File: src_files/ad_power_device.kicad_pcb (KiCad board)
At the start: 2 copper layers, 88.9 x 56.6 mm, 199 parts, among them J1 SPEAKER, J2 5622-6309-ML, U1 RK3566, U2 RK809, U3 AP6256, U4 LPDDRS_32_IS43LQ32128A-062BLI, U5 TLV62569DDC, U6 TLV62569DDC, Y1 32.768KHz, Y2 37.4MHz_10PPM, Y3 24MHz/10ppm

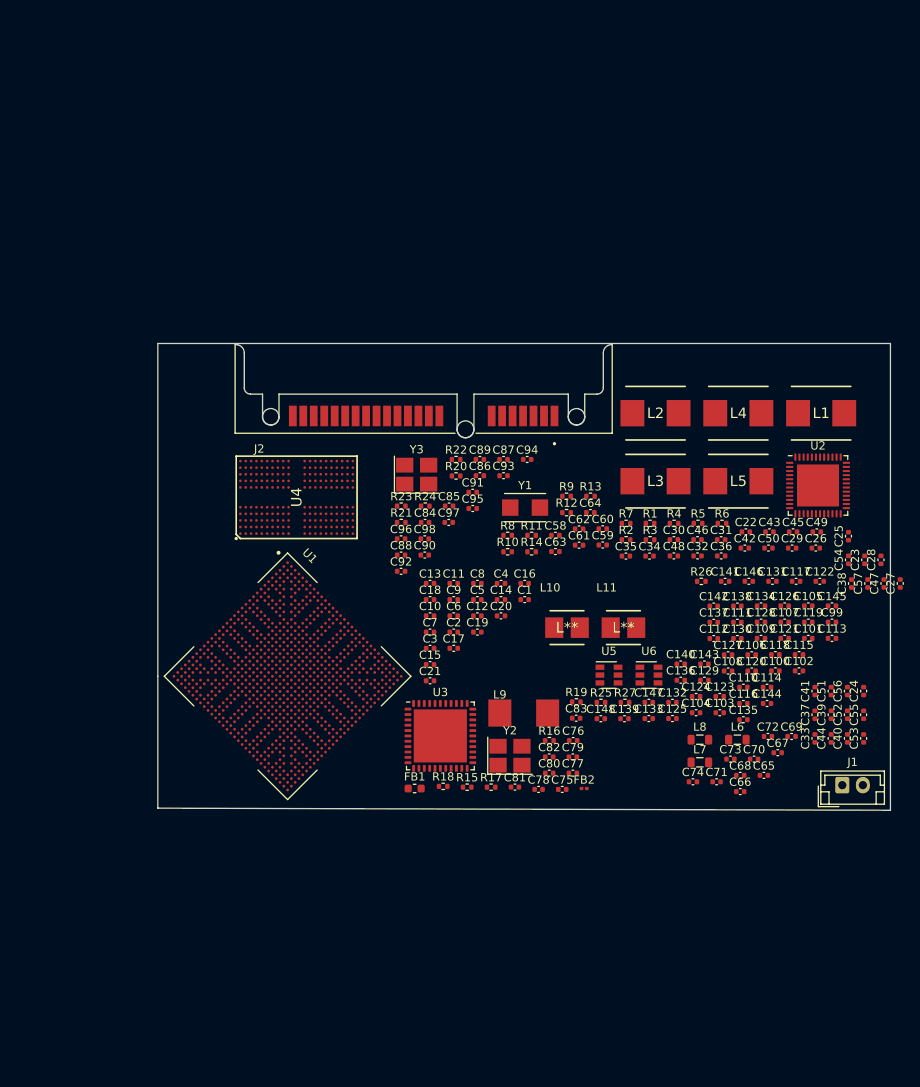
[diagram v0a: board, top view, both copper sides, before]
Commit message: added 3 screens
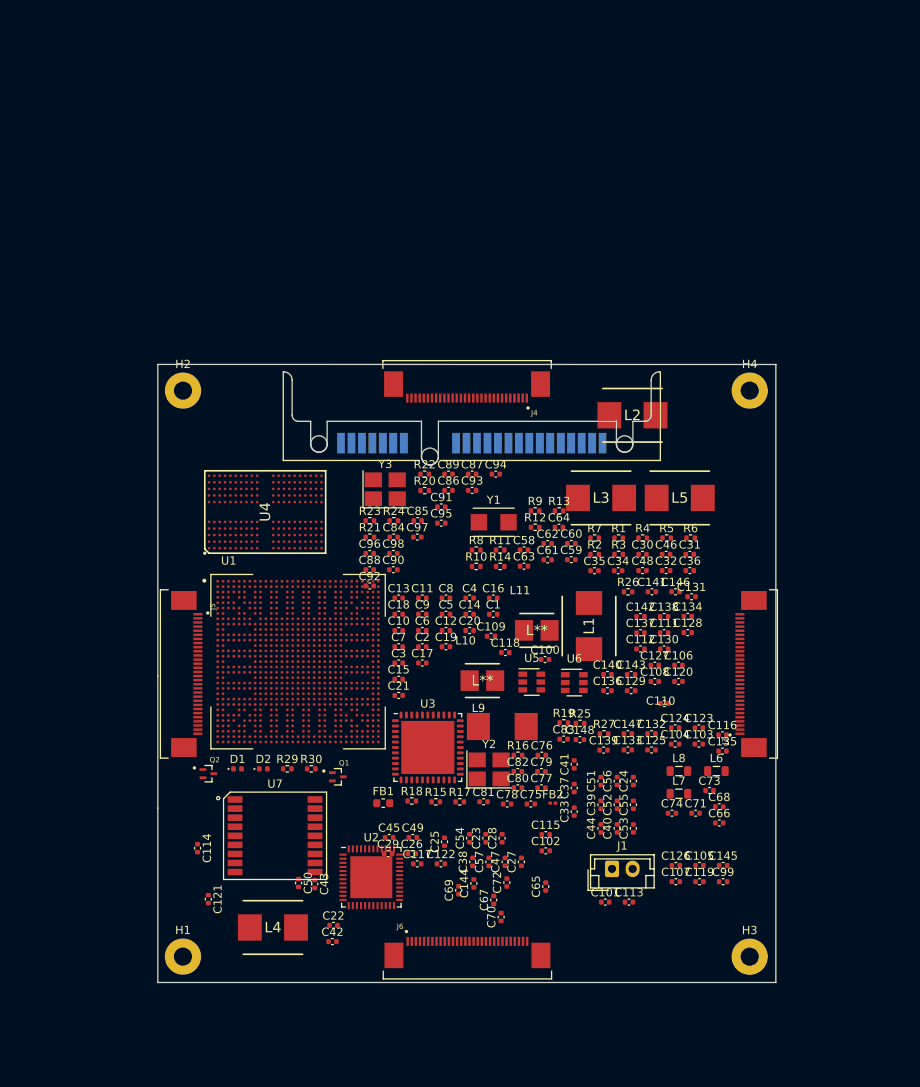
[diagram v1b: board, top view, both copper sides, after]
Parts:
- added D1: LED, LED_SMD:LED_0402_1005Metric, F.Cu at (22.4, 192.6)
- added D2: LED, LED_SMD:LED_0402_1005Metric, F.Cu at (25.5, 192.6)
- added H1: MountingHole, MountingHole:MountingHole_2.2mm_M2_Pad, F.Cu at (15.8, 215.4)
- added H2: MountingHole, MountingHole:MountingHole_2.2mm_M2_Pad, F.Cu at (15.8, 146.7)
- added H3: MountingHole, MountingHole:MountingHole_2.2mm_M2_Pad, F.Cu at (84.5, 215.4)
- added H4: MountingHole, MountingHole:MountingHole_2.2mm_M2_Pad, F.Cu at (84.5, 146.7)
- added J3: 3-1734592-0, greencharge-footprints:TE_3-1734592-0, F.Cu at (83.3, 181.1)
- added J4: 3-1734592-0, greencharge-footprints:TE_3-1734592-0, F.Cu at (50.2, 147.6)
- added J5: 3-1734592-0, greencharge-footprints:TE_3-1734592-0, F.Cu at (17.6, 181.1)
- added J6: 3-1734592-0, greencharge-footprints:TE_3-1734592-0, F.Cu at (50.3, 213.5)
- added Q1: DTC143ZEBTL, greencharge-footprints:SOTFL50P160X85-3N, F.Cu at (34.5, 193.5)
- added Q2: DTC143ZEBTL, greencharge-footprints:SOTFL50P160X85-3N, F.Cu at (18.8, 193.2)
- added R29: 1K, Resistor_SMD:R_0402_1005Metric, F.Cu at (28.4, 192.6)
- added R30: 1K, Resistor_SMD:R_0402_1005Metric, F.Cu at (31.3, 192.6)
- added U7: QUECTEL_L70-RL, greencharge-footprints:QUECTEL_L70-R, F.Cu at (26.4, 201.2)
- J2: moved to B.Cu
- moved L4 84.2 mm to (26.7, 211.8)
- moved C121 76.8 mm to (18.8, 208.4), turned to 270 degrees
- moved U2 72.1 mm to (38.6, 205.7)
- moved C114 71.8 mm to (17.5, 202.2), turned to 270 degrees
- moved C50 70.0 mm to (29.8, 206.4), turned to 270 degrees
- moved C43 69.8 mm to (31.8, 206.6), turned to 270 degrees
- moved C42 69.2 mm to (33.9, 213.6)
- moved C22 69.2 mm to (34.0, 211.6)
- moved C26 61.5 mm to (43.5, 202.9)
- moved C45 61.5 mm to (40.8, 200.9)
- moved C29 61.5 mm to (40.7, 202.9)
- moved C49 61.5 mm to (43.6, 200.9)
- moved C25 61.5 mm to (47.5, 201.4)
- moved C117 57.4 mm to (44.2, 204.1)
- moved C122 57.4 mm to (47.1, 204.1)
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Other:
- board size 88.9 x 56.6 mm -> 75 x 75 mm

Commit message: schematic capture complete
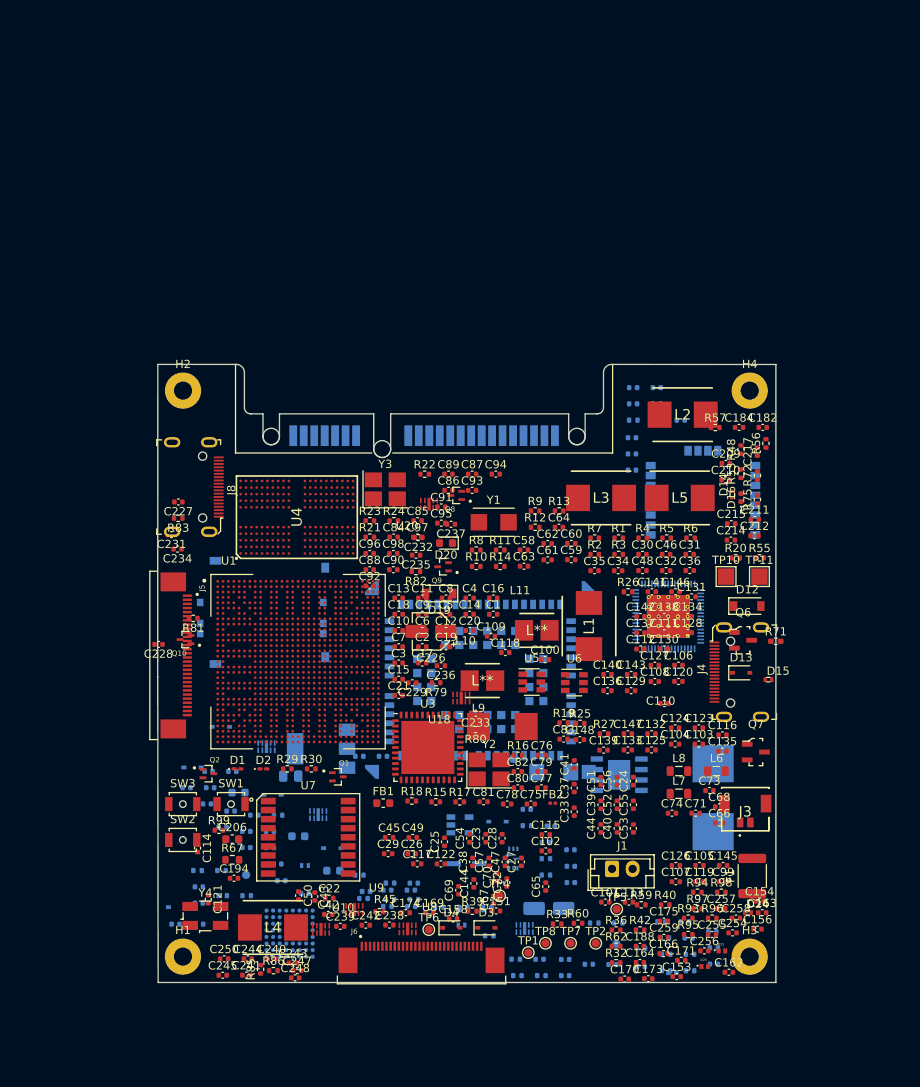
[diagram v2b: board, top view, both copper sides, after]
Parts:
- added C149: 10uF, Capacitor_SMD:C_0402_1005Metric, B.Cu at (70.2, 152.4)
- added C150: 100nF, Capacitor_SMD:C_0402_1005Metric, B.Cu at (73.2, 146.3)
- added C151: 4.7uF, Capacitor_SMD:C_0402_1005Metric, F.Cu at (53.8, 209.8)
- added C152: 4.7uF, Capacitor_SMD:C_0402_1005Metric, B.Cu at (76.7, 211.1)
- added C153: 1uF, Capacitor_SMD:C_0402_1005Metric, F.Cu at (75.7, 217.8)
- added C154: 1uF, Capacitor_SMD:C_0402_1005Metric, F.Cu at (85.7, 208.6)
- added C155: 1uF, Capacitor_SMD:C_0402_1005Metric, B.Cu at (75.1, 217.3)
- added C156: 1uF, Capacitor_SMD:C_0402_1005Metric, F.Cu at (85.5, 212.0)
- added C157: 100nF, Capacitor_SMD:C_0402_1005Metric, B.Cu at (67.9, 216.3)
- added C158: 100nF, Capacitor_SMD:C_0402_1005Metric, F.Cu at (48.5, 210.8)
- added C159: 100nF, Capacitor_SMD:C_0402_1005Metric, B.Cu at (71.3, 216.6)
- added C160: 100nF, Capacitor_SMD:C_0402_1005Metric, B.Cu at (17.7, 211.4)
- added C161: 100nF, Capacitor_SMD:C_0402_1005Metric, B.Cu at (62.1, 215.7)
- added C162: 100nF, Capacitor_SMD:C_0402_1005Metric, F.Cu at (82.0, 217.3)
- added C163: 100nF, Capacitor_SMD:C_0402_1005Metric, F.Cu at (86.0, 210.0)
- added C164: 10uF, Capacitor_SMD:C_0402_1005Metric, F.Cu at (71.2, 216.1)
- added C165: 10uF, Capacitor_SMD:C_0402_1005Metric, B.Cu at (65.0, 216.3)
- added C166: 100nF, Capacitor_SMD:C_0402_1005Metric, F.Cu at (74.1, 215.0)
- added C167: 10uF, Capacitor_SMD:C_0402_1005Metric, B.Cu at (80.0, 212.3)
- added C168: 100nF, Capacitor_SMD:C_0402_1005Metric, B.Cu at (14.9, 211.4)
- added C169: 10uF, Capacitor_SMD:C_0402_1005Metric, F.Cu at (45.7, 210.0)
- added C170: 100nF, Capacitor_SMD:C_0402_1005Metric, F.Cu at (69.4, 218.1)
- added C171: 100nF, Capacitor_SMD:C_0402_1005Metric, F.Cu at (76.2, 215.8)
- added C172: 100nF, Capacitor_SMD:C_0402_1005Metric, B.Cu at (80.2, 214.3)
- added C173: 100nF, Capacitor_SMD:C_0402_1005Metric, F.Cu at (72.2, 218.1)
- added C174: 100nF, Capacitor_SMD:C_0402_1005Metric, F.Cu at (42.8, 210.0)
- added C175: 100nF, Capacitor_SMD:C_0402_1005Metric, F.Cu at (74.1, 211.1)
- added C176: 1uF, Capacitor_SMD:C_0402_1005Metric, B.Cu at (62.1, 217.7)
- added C177: 100nF, Capacitor_SMD:C_0402_1005Metric, B.Cu at (76.2, 150.3)
- added C178: 220pF, Capacitor_SMD:C_0402_1005Metric, B.Cu at (70.2, 154.4)
- added C179: 220pF, Capacitor_SMD:C_0402_1005Metric, B.Cu at (73.2, 148.3)
- added C180: 180pF, Capacitor_SMD:C_0402_1005Metric, B.Cu at (70.4, 146.3)
- added C181: 180pF, Capacitor_SMD:C_0402_1005Metric, B.Cu at (70.2, 156.3)
- added C182: 66pF, Capacitor_SMD:C_0402_1005Metric, F.Cu at (86.1, 151.2)
- added C183: 100nF, Capacitor_SMD:C_0402_1005Metric, B.Cu at (73.3, 150.3)
- added C184: 4.7uF, Capacitor_SMD:C_0402_1005Metric, F.Cu at (83.2, 151.2)
- added C185: 100nF, Capacitor_SMD:C_0402_1005Metric, B.Cu at (70.4, 148.3)
- added C186: 4.7uF, Capacitor_SMD:C_0402_1005Metric, B.Cu at (77.1, 213.1)
- added C187: 4.7uF, Capacitor_SMD:C_0402_1005Metric, B.Cu at (80.2, 216.3)
- added C188: 100nF, Capacitor_SMD:C_0402_1005Metric, F.Cu at (71.2, 214.1)
- added C189: 100nF, Capacitor_SMD:C_0402_1005Metric, B.Cu at (59.0, 215.7)
- added C190: 1uF, Capacitor_SMD:C_0402_1005Metric, B.Cu at (73.8, 211.1)
- added C191: 0.1uF, Capacitor_SMD:C_0402_1005Metric, B.Cu at (23.4, 200.2)
- added C192: 0.1uF, Capacitor_SMD:C_0402_1005Metric, B.Cu at (18.7, 196.8)
- added C193: 0.1uF, Capacitor_SMD:C_0402_1005Metric, B.Cu at (20.6, 199.7)
- added C194: 22pF, Capacitor_SMD:C_0402_1005Metric, F.Cu at (21.9, 205.9)
- added C195: 22pF, Capacitor_SMD:C_0402_1005Metric, B.Cu at (16.2, 194.9)
- added C196: 0.1uF, Capacitor_SMD:C_0402_1005Metric, B.Cu at (23.4, 202.1)
- added C197: 0.1uF, Capacitor_SMD:C_0402_1005Metric, B.Cu at (27.2, 204.1)
- added C198: 0.1uf, Capacitor_SMD:C_0402_1005Metric, B.Cu at (27.7, 206.2)
- added C199: 0.1uF, Capacitor_SMD:C_0402_1005Metric, B.Cu at (26.3, 200.2)
- added C200: 0.1uF, Capacitor_SMD:C_0402_1005Metric, B.Cu at (19.1, 194.9)
- added C201: 0.1uF, Capacitor_SMD:C_0402_1005Metric, B.Cu at (21.7, 192.9)
- added C202: 0.1uF, Capacitor_SMD:C_0402_1005Metric, B.Cu at (21.5, 197.7)
- added C203: 0.1uF, Capacitor_SMD:C_0402_1005Metric, B.Cu at (18.9, 192.9)
- added C204: 2.2uF, Capacitor_SMD:C_0402_1005Metric, B.Cu at (24.4, 198.2)
- added C205: 10uF, Capacitor_SMD:C_0603_1608Metric, B.Cu at (29.7, 200.8)
- added C206: 10uF, Capacitor_SMD:C_0603_1608Metric, F.Cu at (21.7, 201.1)
- added C207: 1uF, Capacitor_SMD:C_0402_1005Metric, B.Cu at (26.3, 202.2)
- added C208: 1uF, Capacitor_SMD:C_0402_1005Metric, B.Cu at (30.6, 207.7)
- added C209: 1uF, Capacitor_SMD:C_0402_1005Metric, F.Cu at (81.6, 155.5)
- added C210: 1uF, Capacitor_SMD:C_0402_1005Metric, F.Cu at (81.6, 157.5)
- added C211: 100nF, Capacitor_SMD:C_0402_1005Metric, F.Cu at (85.1, 162.3)
- added C212: 100nF, Capacitor_SMD:C_0402_1005Metric, F.Cu at (85.1, 164.3)
- added C213: 1uF, Capacitor_SMD:C_0402_1005Metric, B.Cu at (43.4, 207.3)
- added C214: 1uF, Capacitor_SMD:C_0402_1005Metric, F.Cu at (82.2, 164.8)
- added C215: 100nF, Capacitor_SMD:C_0402_1005Metric, F.Cu at (82.3, 162.8)
- added C216: 100nF, Capacitor_SMD:C_0402_1005Metric, B.Cu at (43.5, 209.3)
- added C217: 100nF, Capacitor_SMD:C_0402_1005Metric, F.Cu at (85.4, 154.1)
- added C218: 100nF, Capacitor_SMD:C_0402_1005Metric, B.Cu at (40.5, 207.3)
- added C219: 1uF, Capacitor_SMD:C_0402_1005Metric, B.Cu at (43.8, 206.5)
- added C220: 10uF, Capacitor_SMD:C_0402_1005Metric, B.Cu at (62.8, 206.4)
- added C221: 10uF, Capacitor_SMD:C_0402_1005Metric, B.Cu at (59.8, 201.5)
- added C222: 22uF, Capacitor_SMD:C_0402_1005Metric, B.Cu at (62.8, 204.4)
- added C223: 22uF, Capacitor_SMD:C_0402_1005Metric, B.Cu at (57.5, 197.5)
- added C224: 22uF, Capacitor_SMD:C_0402_1005Metric, B.Cu at (60.4, 199.5)
- added C225: 22uF, Capacitor_SMD:C_0402_1005Metric, B.Cu at (62.8, 202.4)
- added C226: 100uF, Capacitor_SMD:CP_Elec_4x3, F.Cu at (45.8, 175.9)
- added C227: 100nF, Capacitor_SMD:C_0402_1005Metric, F.Cu at (15.2, 160.2)
- added C228: 33pF, Capacitor_SMD:C_0402_1005Metric, F.Cu at (12.8, 177.5)
- added C229: 10pF, Capacitor_SMD:C_0402_1005Metric, F.Cu at (43.6, 182.1)
- added C230: 100uF, Capacitor_SMD:CP_Elec_4x3, B.Cu at (60.2, 209.5)
- added C231: 100nF, Capacitor_SMD:C_0402_1005Metric, F.Cu at (14.4, 164.2)
- added C232: 33pF, Capacitor_SMD:C_0402_1005Metric, F.Cu at (44.3, 164.5)
- added C233: 10pF, Capacitor_SMD:C_0402_1005Metric, F.Cu at (51.3, 185.8)
- added C234: 33pF, Capacitor_SMD:C_0402_1005Metric, F.Cu at (15.1, 165.9)
- added C235: 33pF, Capacitor_SMD:C_0402_1005Metric, F.Cu at (44.0, 166.7)
- added C236: 100nF, Capacitor_SMD:C_0402_1005Metric, F.Cu at (47.1, 180.1)
- added C237: 33pF, Capacitor_SMD:C_0402_1005Metric, F.Cu at (48.3, 162.9)
- added C238: 100nF, Capacitor_SMD:C_0402_1005Metric, F.Cu at (40.8, 211.5)
- added C239: 4.7uF, Capacitor_SMD:C_0402_1005Metric, F.Cu at (34.8, 211.7)
- added C240: 100nF, Capacitor_SMD:C_0402_1005Metric, F.Cu at (26.5, 215.6)
- added C241: 100nF, Capacitor_SMD:C_0402_1005Metric, F.Cu at (23.4, 217.6)
- added C242: 4.7uF, Capacitor_SMD:C_0402_1005Metric, F.Cu at (37.9, 211.6)
- added C243: 100nF, Capacitor_SMD:C_0402_1005Metric, F.Cu at (29.1, 216.2)
- added C244: 100nF, Capacitor_SMD:C_0402_1005Metric, F.Cu at (23.6, 215.6)
- added C245: 100nF, Capacitor_SMD:C_0402_1005Metric, F.Cu at (20.6, 217.6)
- added C246: 1nF_50V, Capacitor_SMD:C_0402_1005Metric, B.Cu at (17.7, 208.9)
- added C247: 1nF_50V, Capacitor_SMD:C_0402_1005Metric, F.Cu at (29.6, 217.1)
- added C248: 1nF_50V, Capacitor_SMD:C_0402_1005Metric, F.Cu at (29.4, 217.9)
- added C249: 1nF_50V, Capacitor_SMD:C_0402_1005Metric, B.Cu at (17.7, 206.9)
- added C250: 100nF, Capacitor_SMD:C_0402_1005Metric, F.Cu at (20.8, 215.6)
- added C251: 130pF, Capacitor_SMD:C_0402_1005Metric, B.Cu at (42.9, 191.1)
- added C252: 1uF, Capacitor_SMD:C_0402_1005Metric, B.Cu at (37.2, 191.1)
- added C253: 1uF, Capacitor_SMD:C_0402_1005Metric, B.Cu at (40.0, 191.1)
- added C254: 47uF_10V, Capacitor_SMD:C_0402_1005Metric, F.Cu at (82.4, 212.5)
- added C255: 47uF_10V, Capacitor_SMD:C_0402_1005Metric, F.Cu at (80.0, 212.7)
- added C256: 22uF_10V, Capacitor_SMD:C_0402_1005Metric, F.Cu at (79.0, 214.7)
- added C257: 22uF_10V, Capacitor_SMD:C_0402_1005Metric, F.Cu at (81.1, 209.5)
- added C258: 100nF, Capacitor_SMD:C_0402_1005Metric, F.Cu at (82.9, 210.7)
- added C259: 100nF, Capacitor_SMD:C_0402_1005Metric, F.Cu at (74.1, 213.0)
- added D10: 1N5819WS, Diode_SMD:D_SOD-323, B.Cu at (16.9, 192.4)
- added D11: ESD5451R-2/TR, greencharge-footprints:DFP1006-2L, B.Cu at (29.4, 202.8)
- added D12: SMF11A, Diode_SMD:D_SOD-123, F.Cu at (84.2, 172.8)
- added D13: 1N5819WS, Diode_SMD:D_SOD-323, F.Cu at (83.5, 180.9)
- added D14: ESD5451R-2/TR, greencharge-footprints:DFP1006-2L, F.Cu at (80.9, 158.1)
- added D15: ESD5451R-2/TR, greencharge-footprints:DFP1006-2L, F.Cu at (88.0, 180.2)
- added D16: LED, LED_SMD:LED_0402_1005Metric, F.Cu at (83.5, 159.7)
- added D17: LED, LED_SMD:LED_0402_1005Metric, B.Cu at (38.0, 207.5)
- added D18: D, Diode_SMD:D_SOD-323, B.Cu at (53.9, 199.0)
- added D19: SMF11A, Diode_SMD:D_SOD-123, F.Cu at (46.8, 171.3)
- added D20: LED, LED_SMD:LED_0603_1608Metric, F.Cu at (47.7, 165.2)
- added D21: SS56, greencharge-footprints:SMAG, B.Cu at (62.8, 193.0)
- added D22: LED, LED_SMD:LED_0603_1608Metric, B.Cu at (55.1, 191.4)
- added D23: ESD9X5VU, greencharge-footprints:ESD9X5VU_DFN1006-2, F.Cu at (81.1, 214.7)
- added D24: ESD5451R-2/TR, greencharge-footprints:DFP1006-2L, F.Cu at (85.5, 208.5)
- added D25: ESD9X5VU, greencharge-footprints:ESD9X5VU_DFN1006-2, F.Cu at (79.0, 216.6)
- added D3: 1N5819WS, Diode_SMD:D_SOD-323, F.Cu at (52.6, 211.9)
- added D4: 1N5819WS, Diode_SMD:D_SOD-323, F.Cu at (48.3, 211.9)
- added D5: 1N5819WS, Diode_SMD:D_SOD-323, B.Cu at (15.0, 209.4)
- added D6: ESD5451R-2/TR, greencharge-footprints:DFP1006-2L, B.Cu at (50.7, 213.1)
- added D7: D, Diode_SMD:D_SOD-323, B.Cu at (20.3, 187.5)
- added D8: D, Diode_SMD:D_SOD-323, B.Cu at (33.9, 202.2)
- added D9: D, Diode_SMD:D_SOD-323, B.Cu at (26.6, 195.7)
- added F1: mSMD300, Fuse:Fuse_1812_4532Metric, F.Cu at (84.8, 205.6)
- added FB3: Ferrite Bead, Inductor_SMD:L_0603_1608Metric, B.Cu at (22.5, 195.5)
- added FB4: Ferrite Bead, Inductor_SMD:L_0603_1608Metric, B.Cu at (34.0, 204.9)
- added IC1: TPS62867RQYR, greencharge-footprints:TPS62865RQYR, B.Cu at (55.8, 203.5)
- added J8: 2001-1-2-21-00-BK, digikey-footprints:HDMI_Mini_Female_2001-1-2-21-00-BK, F.Cu at (20.1, 158.4)
- added J9: SIM_Card, greencharge-footprints:MOLEX_78800-0001, B.Cu at (26.1, 173.6)
- added L12: IHLP1212AEERR22M11, greencharge-footprints:INDPM3630X150N, B.Cu at (50.1, 204.1)
- added L13: 6uH, greencharge-footprints:7443550600, B.Cu at (80.1, 192.0)
- added Q10: DTC143ZEBTL, greencharge-footprints:SOTFL50P160X85-3N, F.Cu at (16.1, 176.9)
- added Q6: DTC143ZEBTL, digikey-footprints:SOT-23-3, F.Cu at (83.7, 177.0)
- added Q7: DTC143ZEBTL, digikey-footprints:SOT-23-3, F.Cu at (85.3, 190.6)
- added Q8: DTC143ZEBTL, greencharge-footprints:SOTFL50P160X85-3N, F.Cu at (48.9, 159.4)
- added Q9: DTC143ZEBTL, greencharge-footprints:SOTFL50P160X85-3N, F.Cu at (47.3, 168.1)
- added R31: 0R, Resistor_SMD:R_0402_1005Metric, B.Cu at (71.3, 214.3)
- added R32: 0R, Resistor_SMD:R_0402_1005Metric, F.Cu at (68.3, 216.1)
- added R33: 1R_1%, Resistor_SMD:R_0402_1005Metric, F.Cu at (61.2, 211.4)
- added R34: 1R_1%, Resistor_SMD:R_0402_1005Metric, B.Cu at (56.3, 217.7)
- added R35: 1R_1%, Resistor_SMD:R_0402_1005Metric, B.Cu at (52.7, 209.7)
- added R36: 1R_1%, Resistor_SMD:R_0402_1005Metric, F.Cu at (68.3, 212.1)
- added R37: 2.2R_5%, Resistor_SMD:R_0402_1005Metric, B.Cu at (49.8, 209.7)
- added R38: 2.2R_5%, Resistor_SMD:R_0402_1005Metric, B.Cu at (52.9, 212.8)
- added R39: 2.2R_5%, Resistor_SMD:R_0402_1005Metric, F.Cu at (50.9, 209.9)
- added R40: 2.2R_5%, Resistor_SMD:R_0402_1005Metric, F.Cu at (74.3, 209.1)
- added R41: 2.2R_5%, Resistor_SMD:R_0402_1005Metric, B.Cu at (77.3, 215.1)
- added R42: 2.2R_5%, Resistor_SMD:R_0402_1005Metric, F.Cu at (71.2, 212.1)
- added R43: 2.2R_5%, Resistor_SMD:R_0402_1005Metric, B.Cu at (56.1, 215.7)
- added R44: 2.2R_5%, Resistor_SMD:R_0402_1005Metric, B.Cu at (59.2, 217.7)
- added R45: 1.62K_1%, Resistor_SMD:R_0402_1005Metric, F.Cu at (39.6, 209.9)
- added R46: 1K, Resistor_SMD:R_0402_1005Metric, B.Cu at (65.7, 211.3)
- added R47: 100K, Resistor_SMD:R_0402_1005Metric, B.Cu at (74.4, 217.1)
- added R48: 2.2K_5%, Resistor_SMD:R_0402_1005Metric, F.Cu at (83.5, 153.9)
- added R49: 2.2K_5%, Resistor_SMD:R_0402_1005Metric, B.Cu at (40.6, 209.3)
- added R50: 2.2K_5%, Resistor_SMD:R_0402_1005Metric, B.Cu at (43.8, 208.4)
- added R51: 2.2K_5%, Resistor_SMD:R_0402_1005Metric, B.Cu at (40.9, 206.4)
- added R52: 2.2K_5%, Resistor_SMD:R_0402_1005Metric, B.Cu at (37.7, 208.3)
- added R53: 2.2K_5%, Resistor_SMD:R_0402_1005Metric, F.Cu at (83.5, 156.8)
- added R54: 0R, Resistor_SMD:R_0402_1005Metric, B.Cu at (70.4, 150.3)
- added R55: 0R, Resistor_SMD:R_0402_1005Metric, F.Cu at (85.7, 167.0)
- added R56: 4.7K, Resistor_SMD:R_0402_1005Metric, F.Cu at (86.5, 153.1)
- added R57: 1K, Resistor_SMD:R_0402_1005Metric, F.Cu at (80.3, 151.2)
- added R58: 0R, Resistor_SMD:R_0402_1005Metric, B.Cu at (68.6, 211.3)
- added R59: 0R, Resistor_SMD:R_0402_1005Metric, F.Cu at (71.4, 209.1)
- added R60: 10K, Resistor_SMD:R_0402_1005Metric, F.Cu at (63.7, 211.3)
- added R61: 10K, Resistor_SMD:R_0402_1005Metric, B.Cu at (74.4, 215.1)
- added R62: 27K, Resistor_SMD:R_0402_1005Metric, F.Cu at (68.3, 214.1)
- added R63: 1.8K, Resistor_SMD:R_0402_1005Metric, B.Cu at (77.3, 217.1)
- added R64: 1.8K, Resistor_SMD:R_0402_1005Metric, B.Cu at (74.2, 213.1)
- added R65: 2.2K_402, Resistor_SMD:R_0402_1005Metric, B.Cu at (49.8, 209.4)
- added R66: 100K, Resistor_SMD:R_0805_2012Metric, B.Cu at (28.8, 193.5)
- added R67: 249OHM/1%, Resistor_SMD:R_0603_1608Metric, F.Cu at (21.7, 203.6)
- added R68: 4.7K, Resistor_SMD:R_0402_1005Metric, B.Cu at (27.3, 198.2)
- added R69: 4.7K, Resistor_SMD:R_0402_1005Metric, B.Cu at (52.7, 209.4)
- added R70: 4.7K, Resistor_SMD:R_0402_1005Metric, B.Cu at (46.9, 209.4)
- added R71: 100R, Resistor_SMD:R_0402_1005Metric_Pad0.72x0.64mm_HandSolder, F.Cu at (87.7, 177.1)
- added R72: R_US, Resistor_SMD:R_0402_1005Metric, F.Cu at (85.5, 157.0)
- added R73: 22R, Resistor_SMD:R_0402_1005Metric, B.Cu at (40.9, 208.4)
- added R74: 1K, Resistor_SMD:R_0402_1005Metric, B.Cu at (37.1, 205.5)
- added R75: 1K, Resistor_SMD:R_0402_1005Metric, F.Cu at (85.5, 159.9)
- added R76: 100K, Resistor_SMD:R_0402_1005Metric, B.Cu at (59.8, 205.5)
- added R77: 205K, Resistor_SMD:R_0402_1005Metric, B.Cu at (59.8, 203.5)
- added R78: 6.8K_1%, Resistor_SMD:R_0402_1005Metric, B.Cu at (57.5, 199.5)
- added R79: 0R, Resistor_SMD:R_0402_1005Metric, F.Cu at (46.5, 182.1)
- added R80: 0R, Resistor_SMD:R_0402_1005Metric, F.Cu at (51.3, 187.8)
- added R81: 15K, Resistor_SMD:R_0402_1005Metric, F.Cu at (17.0, 174.3)
- added R82: 0R, Resistor_SMD:R_0402_1005Metric, F.Cu at (44.0, 168.6)
- added R83: 0R, Resistor_SMD:R_0402_1005Metric, F.Cu at (15.2, 162.2)
- added R84: 0.1R, Resistor_SMD:R_0402_1005Metric, B.Cu at (17.5, 204.9)
- added R85: 10K_1%, Resistor_SMD:R_0402_1005Metric, F.Cu at (25.2, 216.9)
- added R86: 10K_1%, Resistor_SMD:R_0402_1005Metric, F.Cu at (26.7, 217.1)
- added R87: 10K_1%, Resistor_SMD:R_0402_1005Metric, B.Cu at (20.4, 204.9)
- added R88: 10K_1%, Resistor_SMD:R_0402_1005Metric, B.Cu at (23.5, 208.0)
- added R89: 0.1R, Resistor_SMD:R_0402_1005Metric, B.Cu at (20.6, 208.0)
- added R90: 1K, Resistor_SMD:R_0402_1005Metric, B.Cu at (45.8, 191.1)
- added R91: 22.6R, Resistor_SMD:R_0402_1005Metric, B.Cu at (48.7, 191.1)
- added R92: 10K, Resistor_SMD:R_0402_1005Metric, B.Cu at (51.6, 191.1)
- added R93: 5.1K, Resistor_SMD:R_0402_1005Metric, F.Cu at (77.1, 210.7)
- added R94: 5.1K, Resistor_SMD:R_0402_1005Metric, F.Cu at (78.2, 207.6)
- added R95: 2.2R, Resistor_SMD:R_0402_1005Metric, F.Cu at (77.1, 212.7)
- added R96: 2.2R, Resistor_SMD:R_0402_1005Metric, F.Cu at (80.0, 210.7)
- added R97: 10K, Resistor_SMD:R_0402_1005Metric, F.Cu at (78.2, 209.6)
- added R98: 15K, Resistor_SMD:R_0402_1005Metric, F.Cu at (81.1, 207.6)
- added R99: 100R, Resistor_SMD:R_0402_1005Metric, F.Cu at (20.1, 200.0)
- added SW1: PWR_ON, Button_Switch_SMD:SW_SPST_B3U-1000P-B, F.Cu at (21.6, 196.9)
- added SW2: RESET BTN, Button_Switch_SMD:SW_SPST_B3U-1000P-B, F.Cu at (15.7, 201.2)
- added SW3: RECOVER BTN, Button_Switch_SMD:SW_SPST_B3U-1000P-B, F.Cu at (15.7, 196.9)
- added TP1: HDMI_TX_AVDD_0V9, TestPoint:TestPoint_Pad_D1.0mm, F.Cu at (57.7, 214.9)
- added TP10: bat+, TestPoint:TestPoint_Pad_2.0x2.0mm, F.Cu at (81.7, 169.3)
- added TP11: bat-, TestPoint:TestPoint_Pad_2.0x2.0mm, F.Cu at (85.7, 169.3)
- added TP2: HDMI_TX_AVDD_1V8, TestPoint:TestPoint_Pad_D1.0mm, F.Cu at (65.8, 213.7)
- added TP3: LVDS_TX0_AVDD_1V8, TestPoint:TestPoint_Pad_D1.0mm, B.Cu at (68.3, 213.8)
- added TP4: LVDS_TX0_AVDD_0V9, TestPoint:TestPoint_Pad_D1.0mm, F.Cu at (54.2, 208.0)
- added TP5: LVDS_TX1_AVDD_0V9, TestPoint:TestPoint_Pad_D1.0mm, F.Cu at (68.4, 209.6)
- added TP6: LVDS_TX1_AVDD_1V8, TestPoint:TestPoint_Pad_D1.0mm, F.Cu at (45.6, 212.1)
- added TP7: EDP_TX_AVDD_0V9, TestPoint:TestPoint_Pad_D1.0mm, F.Cu at (62.8, 213.7)
- added TP8: EDP_TX_AVDD_1V8, TestPoint:TestPoint_Pad_D1.0mm, F.Cu at (59.7, 213.7)
- added TP9: USB_OTG_ID, TestPoint:TestPoint_Pad_D1.0mm, B.Cu at (23.4, 205.5)
- added U10: ESD5304D-TP, greencharge-footprints:ESD5304D-TP, F.Cu at (35.2, 208.9)
- added U11: NFC_VS1797SM, greencharge-footprints:VS1797SM, B.Cu at (85.2, 155.8)
- added U12: MCDP2900, greencharge-footprints:BGA-64_8x8_7.0x7.0mm_MCDP2900, B.Cu at (28.7, 212.6)
- added U13: ZLDO1117G12TA, Package_TO_SOT_SMD:SOT-223-3_TabPin2, B.Cu at (32.5, 190.1)
- added U14: ESD5304D-TP, greencharge-footprints:ESD5304D-TP, B.Cu at (23.2, 186.8)
- added U15: ESD5304D-TP, greencharge-footprints:ESD5304D-TP, B.Cu at (29.5, 195.0)
- added U16: ESD5304D-TP, greencharge-footprints:ESD5304D-TP, B.Cu at (59.9, 215.1)
- added U17: SY6280AAAC, Package_TO_SOT_SMD:SOT-23-5, B.Cu at (49.4, 199.4)
- added U18: ESD5304D-TP, greencharge-footprints:ESD5304D-TP, F.Cu at (46.9, 187.1)
- added U19: quesctel_EG91-EX, greencharge-footprints:XCVR_EG91EFB-512-SNND, B.Cu at (51.8, 181.8)
- added U20: ESD5304D-TP, greencharge-footprints:ESD5304D-TP, F.Cu at (42.9, 163.6)
- added U21: SY6912A, Package_SO:Diodes_PSOP-8, B.Cu at (68.7, 193.3)
- added U8: ESD5304D-TP, greencharge-footprints:ESD5304D-TP, F.Cu at (45.7, 208.9)
- added U9: ESD5304D-TP, greencharge-footprints:ESD5304D-TP, F.Cu at (39.2, 206.5)
- added Y4: 27MHz, Crystal:Crystal_SMD_EuroQuartz_MJ-4Pin_5.0x3.2mm, F.Cu at (18.5, 210.4)
- C40, C41, C42, C43, C44, C47, C50, C52, C54: value 1U -> 1uF
- C51: value 4.7u -> 4.7uF
- C55: value 10u -> 10uF
- D1, D2: footprint LED_SMD:LED_0402_1005Metric -> LED_SMD:LED_0201_0603Metric_Pad0.64x0.40mm_HandSolder
- J3: value 3-1734592-0 -> 205957-0271; footprint greencharge-footprints:TE_3-1734592-0 -> greencharge-footprints:2059570271
- J4: value 3-1734592-0 -> 2001-1-2-21-00-BK; footprint greencharge-footprints:TE_3-1734592-0 -> digikey-footprints:HDMI_Mini_Female_2001-1-2-21-00-BK
- R20: value 0R -> 4.7K
- U2: footprint Package_DFN_QFN:TQFN-48-1EP_7x7mm_P0.5mm_EP5.1x5.1mm -> Package_DFN_QFN:QFN-68-1EP_8x8mm_P0.4mm_EP5.2x5.2mm_ThermalVias; moved to B.Cu
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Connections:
- C41 pad 1: (no net) -> VCCA_1V8
- C42 pad 1: (no net) -> VDDA0V9_IMAGE
- C43 pad 1: (no net) -> VCCA1V8_PMU
- C44 pad 1: (no net) -> VDDA_0V9
- C47 pad 1: (no net) -> VCCA1V8_IMAGE
- C50 pad 1: (no net) -> VDDA0V9_PMU
- C51 pad 1: (no net) -> VCCIO_ACODEC
- C52 pad 1: (no net) -> VCC3V3_SD
- C54 pad 1: (no net) -> VCCIO_SD
- C55 pad 1: (no net) -> VCC_3V3
- C60 pad 2: /RK890_IC_AUXILLARY/RESETn -> /RESETn
- C61 pad 1: (no net) -> Net-(C61-Pad1)
- C63 pad 2: (no net) -> /RK890_IC_AUXILLARY/PMIC_PWRON
- C66 pad 1: (no net) -> Net-(C66-Pad1)
- C66 pad 2: (no net) -> Net-(C66-Pad2)
- C67 pad 1: (no net) -> Net-(C67-Pad1)
- C68 pad 1: (no net) -> Net-(C68-Pad1)
- C69 pad 1: (no net) -> Net-(C69-Pad1)
- C70 pad 1: (no net) -> Net-(C70-Pad1)
- C71 pad 1: (no net) -> Net-(C71-Pad1)
- C72 pad 1: (no net) -> Net-(C72-Pad1)
- J2 pad P1: +3V3 -> VCC_3V3
- J2 pad P2: +3V3 -> VCC_3V3
- J2 pad P3: +3V3 -> VCC_3V3
- J3 pad 1: (no net) -> /RF1
- J3 pad 2: (no net) -> /RF2
- J4 pad 1: (no net) -> /RK3566_PART_C/HDMI_TX2P_PORT+
- J4 pad 10: (no net) -> /RK3566_PART_C/HDMI_TXCLKP_PORT+
- J4 pad 11: (no net) -> GND
- J4 pad 12: (no net) -> /RK3566_PART_C/HDMI_TXCLKN_PORT-
- J4 pad 13: (no net) -> /RK3566_PART_C/HDMI_TX_CEC_PORT
- J4 pad 15: (no net) -> /RK3566_PART_C/HDMI_TXDDC_SCL_PORT
- J4 pad 16: (no net) -> /RK3566_PART_C/HDMI_TXDDC_SDA_PORT
- J4 pad 17: (no net) -> GND
- J4 pad 18: (no net) -> /RK3566_PART_C/VCC5V_HDMI_TX
- J4 pad 19: (no net) -> /RK3566_PART_C/HDMI_TX_HPD_PORT
- J4 pad 2: (no net) -> GND
- J4 pad 3: (no net) -> /RK3566_PART_C/HDMI_TX2N_PORT-
- J4 pad 4: (no net) -> /RK3566_PART_C/HDMI_TX1P_PORT+
- J4 pad 5: (no net) -> GND
- J4 pad 6: (no net) -> /RK3566_PART_C/HDMI_TX1N_PORT-
- J4 pad 7: (no net) -> /RK3566_PART_C/HDMI_TX0P_PORT+
- J4 pad 8: (no net) -> GND
- J4 pad 9: (no net) -> /RK3566_PART_C/HDMI_TX0N_PORT-
- J5 pad 1: (no net) -> +5V
- J5 pad 15: (no net) -> GND
- J5 pad 18: (no net) -> GND
- J5 pad 2: (no net) -> +5V
- J5 pad 21: (no net) -> GND
- J5 pad 24: (no net) -> GND
- J5 pad 27: (no net) -> GND
- J5 pad 3: (no net) -> +5V
- J5 pad 30: (no net) -> GND
- J5 pad 4: (no net) -> GND
- J5 pad 6: (no net) -> VCC3V3_EXT
- J5 pad 7: (no net) -> /I2C2_SDA_M0_TP
- J5 pad 8: (no net) -> /I2C2_SCL_M0_TP
- J5 pad S1: Net-(J5-PadS1) -> GND
- J5 pad S2: Net-(J5-PadS1) -> GND
- J6 pad 1: (no net) -> +5V
- J6 pad 11: (no net) -> /BL_EN_GPIO1_B7_DISPLAY_ONE
- J6 pad 14: (no net) -> /TP_RST_L_GPIO1_C2_DISPLAY_ONE
- J6 pad 15: (no net) -> GND
- J6 pad 18: (no net) -> GND
- J6 pad 2: (no net) -> +5V
- J6 pad 21: (no net) -> GND
- J6 pad 24: (no net) -> GND
- J6 pad 27: (no net) -> GND
- J6 pad 3: (no net) -> +5V
- J6 pad 30: (no net) -> GND
- J6 pad 4: (no net) -> GND
- J6 pad 6: (no net) -> VCC3V3_EXT
- J6 pad 7: (no net) -> /I2C2_SDA_M0_TP
- J6 pad 8: (no net) -> /I2C2_SCL_M0_TP
- J6 pad 9: (no net) -> /LCD_1_EN_GPIO1_B5_C7
- J6 pad S1: Net-(J6-PadS1) -> GND
- J6 pad S2: Net-(J6-PadS1) -> GND
- L1 pad 2: (no net) -> /RK809_IC_DCDC/SW2
- L2 pad 2: (no net) -> /RK809_IC_DCDC/SW1
- L3 pad 2: (no net) -> /RK809_IC_DCDC/SW5
- L4 pad 2: (no net) -> /RK809_IC_DCDC/SW4
- L5 pad 2: (no net) -> /RK809_IC_DCDC/SW3
- L8 pad 1: (no net) -> Net-(L8-Pad1)
- R10 pad 1: (no net) -> Net-(R10-Pad1)
- R11 pad 1: (no net) -> /RK890_IC_AUXILLARY/RST_KEY
- R11 pad 2: /RK890_IC_AUXILLARY/RESETn -> /RESETn
- R12 pad 2: /RK890_IC_AUXILLARY/PMIC_EXT_EN -> /PMIC_EXT_EN
- R20 pad 1: (no net) -> /NFC_SDA
- R20 pad 2: (no net) -> VCC3V3_PMU
- R3 pad 2: (no net) -> /RK809_IC_DCDC/FB1
- R4 pad 1: (no net) -> /RK809_IC_DCDC/FB5
- R8 pad 1: (no net) -> VCCIO_WL
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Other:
- outline, holes or cut-outs redrawn

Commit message: schematic capture complete
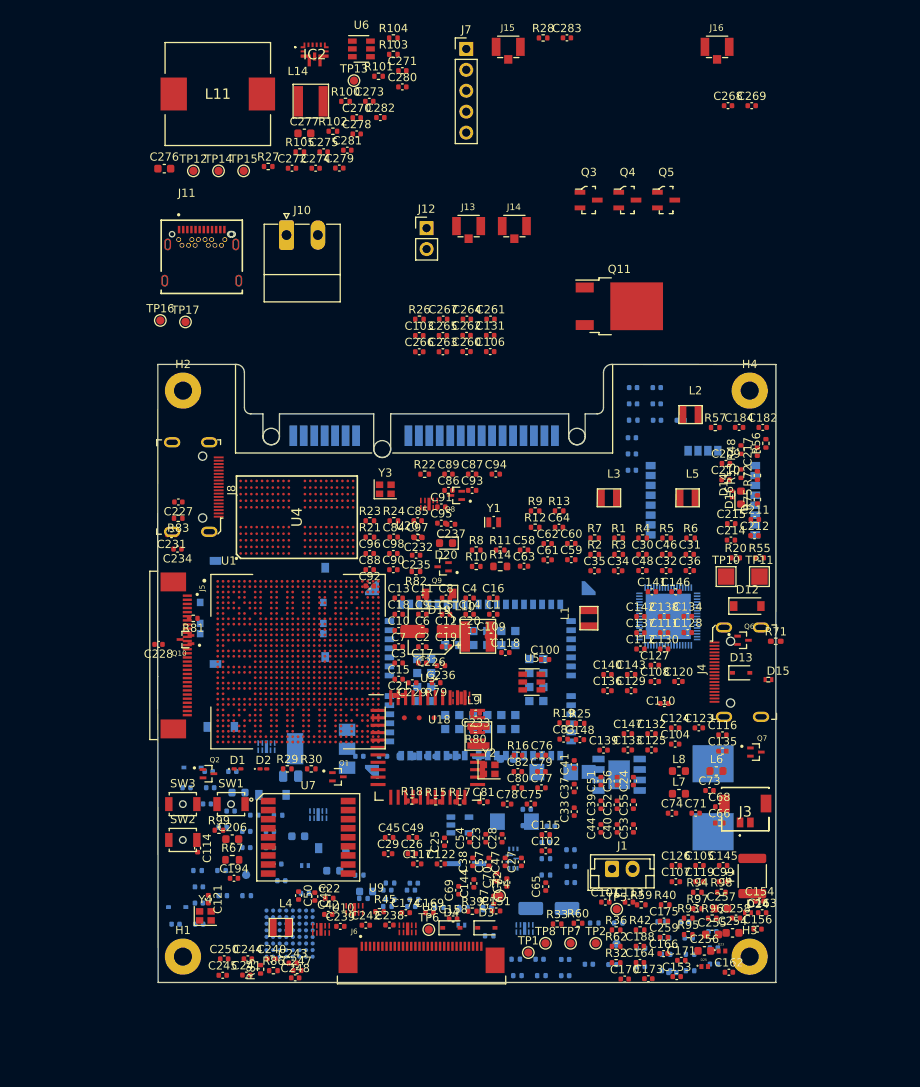
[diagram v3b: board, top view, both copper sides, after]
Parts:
- removed FB1: Ferrite_Bead_Small, Inductor_SMD:L_0603_1608Metric
- removed FB2: Ferrite_Bead_Small, Inductor_SMD:L_0201_0603Metric
- added C260: 100nF, Capacitor_SMD:C_0402_1005Metric, F.Cu at (50.2, 142.0)
- added C261: 100nF, Capacitor_SMD:C_0402_1005Metric, F.Cu at (53.1, 138.0)
- added C262: 100nF, Capacitor_SMD:C_0402_1005Metric, F.Cu at (50.2, 140.0)
- added C263: 100nF, Capacitor_SMD:C_0402_1005Metric, F.Cu at (47.3, 142.0)
- added C264: 100nF, Capacitor_SMD:C_0402_1005Metric, F.Cu at (50.2, 138.0)
- added C265: 100nF, Capacitor_SMD:C_0402_1005Metric, F.Cu at (47.3, 140.0)
- added C266: 100nF, Capacitor_SMD:C_0402_1005Metric, F.Cu at (44.4, 142.0)
- added C267: 100nF, Capacitor_SMD:C_0402_1005Metric, F.Cu at (47.3, 138.0)
- added C268: 27pF_50V, Capacitor_SMD:C_0402_1005Metric, F.Cu at (81.9, 112.1)
- added C269: 27pF_50V, Capacitor_SMD:C_0402_1005Metric, F.Cu at (84.8, 112.1)
- added C270: 10uF, Capacitor_SMD:C_0402_1005Metric, F.Cu at (36.8, 113.6)
- added C271: 100nF, Capacitor_SMD:C_0402_1005Metric, F.Cu at (42.4, 107.9)
- added C272: 100NF, Capacitor_SMD:C_0402_1005Metric, F.Cu at (29.0, 119.7)
- added C273: 2.2uF, Capacitor_SMD:C_0402_1005Metric, F.Cu at (38.4, 111.6)
- added C274: 39nF, Capacitor_SMD:C_0402_1005Metric, F.Cu at (31.9, 119.7)
- added C275: 82pF, Capacitor_SMD:C_0402_1005Metric, F.Cu at (32.8, 117.7)
- added C276: 22uF_16V, Capacitor_SMD:C_0603_1608Metric, F.Cu at (13.5, 119.8)
- added C277: 22uF_16V, Capacitor_SMD:C_0603_1608Metric, F.Cu at (30.5, 115.5)
- added C278: 100nF, Capacitor_SMD:C_0402_1005Metric, F.Cu at (36.8, 115.5)
- added C279: 4.7uF, Capacitor_SMD:C_0402_1005Metric, F.Cu at (34.7, 119.7)
- added C280: 10uF, Capacitor_SMD:C_0402_1005Metric, F.Cu at (42.4, 109.8)
- added C281: 10uF, Capacitor_SMD:C_0402_1005Metric, F.Cu at (35.7, 117.5)
- added C282: 10uF, Capacitor_SMD:C_0402_1005Metric, F.Cu at (39.7, 113.6)
- added C283: 100nF, Capacitor_SMD:C_0402_1005Metric, F.Cu at (62.3, 103.9)
- added IC2: TPS61288RQQR, greencharge-footprints:TPS61288RQQR, F.Cu at (31.7, 105.9)
- added J10: Conn_01x02_Male, Connector_Phoenix_MC:PhoenixContact_MC_1,5_2-G-3.81_1x02_P3.81mm_Horizontal, F.Cu at (28.3, 127.8)
- added J11: USB_C_Receptacle, greencharge-footprints:GCT_USB4056-03-A_REVA, F.Cu at (18.0, 133.4)
- added J12: DEBUG_4G, Connector_PinHeader_2.54mm:PinHeader_1x02_P2.54mm_Vertical, F.Cu at (45.3, 127.0)
- added J13: U.FL-R-SMT-1(10), greencharge-footprints:HRS_U.FL-R-SMT-1(10), F.Cu at (50.4, 126.7)
- added J14: U.FL-R-SMT-1(10), greencharge-footprints:HRS_U.FL-R-SMT-1(10), F.Cu at (56.0, 126.7)
- added J15: U.FL-R-SMT-1(10), greencharge-footprints:HRS_U.FL-R-SMT-1(10), F.Cu at (55.2, 105.0)
- added J16: U.FL-R-SMT-1(10), greencharge-footprints:HRS_U.FL-R-SMT-1(10), F.Cu at (80.6, 105.0)
- added J7: Conn_01x05_Male, Connector_PinHeader_2.54mm:PinHeader_1x05_P2.54mm_Vertical, F.Cu at (50.1, 105.2)
- added L14: 2.2uH, greencharge-footprints:WPN4020H2R2MT, F.Cu at (29.8, 111.6)
- added Q11: IRFR9024NTRPBF, Package_TO_SOT_SMD:TO-252-2, F.Cu at (68.7, 136.5)
- added Q3: 2SK3018, digikey-footprints:SOT-23-3, F.Cu at (65.0, 123.6)
- added Q4: 2SK3018, digikey-footprints:SOT-23-3, F.Cu at (69.7, 123.6)
- added Q5: 2SK3018, digikey-footprints:SOT-23-3, F.Cu at (74.4, 123.6)
- added R100: 931K, Resistor_SMD:R_0402_1005Metric, F.Cu at (35.5, 111.6)
- added R101: 48.7K, Resistor_SMD:R_0402_1005Metric, F.Cu at (39.5, 108.5)
- added R102: 20K, Resistor_SMD:R_0402_1005Metric, F.Cu at (33.9, 115.2)
- added R103: 475K, Resistor_SMD:R_0402_1005Metric, F.Cu at (41.3, 105.9)
- added R104: 100K, Resistor_SMD:R_0402_1005Metric, F.Cu at (41.3, 103.9)
- added R105: 100K, Resistor_SMD:R_0402_1005Metric, F.Cu at (29.9, 117.7)
- added R28: 0R, Resistor_SMD:R_0402_1005Metric, F.Cu at (59.5, 103.9)
- added TP12: VDD_CPU, TestPoint:TestPoint_Pad_D1.0mm, F.Cu at (17.0, 120.0)
- added TP13: 3V3, TestPoint:TestPoint_Pad_D1.0mm, F.Cu at (36.5, 109.1)
- added TP14: 12V, TestPoint:TestPoint_Pad_D1.0mm, F.Cu at (20.1, 120.0)
- added TP15: VCC3V3_EXT, TestPoint:TestPoint_Pad_D1.0mm, F.Cu at (23.1, 120.0)
- added TP16: VBUS, TestPoint:TestPoint_Pad_D1.0mm, F.Cu at (13.0, 138.2)
- added TP17: 5V, TestPoint:TestPoint_Pad_D1.0mm, F.Cu at (16.1, 138.4)
- C103: value 1uF -> 100nF
- C106: value 100nF -> 10uF
- C131: value 4.7uF -> 10uF
- C22, C27, C28, C33, C34, C62: value 1U -> 1uF
- C226, C230: footprint Capacitor_SMD:CP_Elec_4x3 -> Capacitor_SMD:CP_Elec_5x5.4
- C251, C254, C255, C256, C257: footprint Capacitor_SMD:C_0402_1005Metric -> Capacitor_SMD:C_0603_1608Metric
- C58, C59: value 1uF -> 22pF
- C63, C64, C78, C87, C88, C89, C90, C91, C92: value 100n -> 100nF
- C65: value 10u_10V -> 10uF_10V
- C66, C68: value 2.2u -> 2.2uF
- C67, C69, C70: value 1u -> 1uF
- C71, C72: value 100n -> 100nF_10V
- C73, C74: value 1n -> 1nF_50V
- D16, D17: footprint LED_SMD:LED_0402_1005Metric -> LED_SMD:LED_0603_1608Metric
- D18: value D -> SS56; footprint Diode_SMD:D_SOD-323 -> greencharge-footprints:SMAG
- D7, D8, D9: footprint Diode_SMD:D_SOD-323 -> Diode_SMD:D_SOD-123
- FB3, FB4: value Ferrite Bead -> MPZ1608S471ATD25
- L1, L2, L3, L4, L5: footprint greencharge-footprints:SRP6540-5R6M -> greencharge-footprints:252010CDMCDDS-R47MC
- L10: footprint 74438357068_ind:74438357068 -> greencharge-footprints:WPN4020H2R2MT
- L11: value 2.2uH -> RLF12560T2R7N110; footprint 74438357068_ind:74438357068 -> greencharge-footprints:RLF12560T2R7N110
- L6, L7, L8: footprint Inductor_SMD:L_0805_2012Metric -> Inductor_SMD:L_0603_1608Metric
- L9: footprint greencharge-footprints:S6125-M2-3.0A -> greencharge-footprints:SNR3015K-3R3M
- Q6, Q7: footprint digikey-footprints:SOT-23-3 -> greencharge-footprints:SOTFL50P160X85-3N
- R14: footprint Resistor_SMD:R_0402_1005Metric -> Resistor_SMD:R_0603_1608Metric
- R26: value 200K -> 0.1R
- R27: value 100K -> 34K
- R72: value R_US -> 0R
- U2: footprint Package_DFN_QFN:QFN-68-1EP_8x8mm_P0.4mm_EP5.2x5.2mm_ThermalVias -> greencharge-footprints:QFN-68_EP_7x7_Pitch0.35mm
- U21: footprint Package_SO:Diodes_PSOP-8 -> Package_SO:Diodes_SO-8EP
- U3: footprint Package_DFN_QFN:QFN-44-1EP_8x8mm_P0.65mm_EP6.45x6.45mm -> greencharge-footprints:ap6256_QFN-44_12.5x12.5_Pitch0.9mm
- U5, U6: value TLV62569DDC -> TLV62569PDDCR
- Y1: footprint Crystal:Crystal_SMD_Qantek_QC5CB-2Pin_5x3.2mm -> Crystal:Crystal_SMD_MicroCrystal_CM9V-T1A-2Pin_1.6x1.0mm
- Y2, Y3: footprint Crystal:Crystal_SMD_3225-4Pin_3.2x2.5mm_HandSoldering -> Crystal:Crystal_SMD_2016-4Pin_2.0x1.6mm
- Y4: footprint Crystal:Crystal_SMD_EuroQuartz_MJ-4Pin_5.0x3.2mm -> Crystal:Crystal_SMD_2016-4Pin_2.0x1.6mm
- moved U6 81.1 mm to (37.4, 105.2)
- moved R27 80.0 mm to (26.1, 119.5)
- moved L11 70.1 mm to (20.0, 110.7)
- moved C103 60.1 mm to (44.4, 140.0)
- moved C106 44.4 mm to (53.0, 142.0)
- moved R26 41.7 mm to (44.4, 138.0)
- moved C131 40.0 mm to (53.0, 140.0)
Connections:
- C103 pad 1: (no net) -> VCC0V6_DDR
- C103 pad 2: (no net) -> GND
- C106 pad 1: (no net) -> VCC1V8_DDR
- C106 pad 2: (no net) -> GND
- C131 pad 1: +3V3 -> VCC1V8_DDR
- C177 pad 1: VCC_3V3 -> VCC3V3_EXT
- C183 pad 1: VCC_3V3 -> VCC3V3_EXT
- C184 pad 1: VCC_3V3 -> VCC3V3_EXT
- C225 pad 1: Net-(C225-Pad1) -> VCC3V3_EXT
- C81 pad 1: VCCIO_W -> VCCIO_WL
- C82 pad 1: VCCIO_W -> VCCIO_WL
- D18 pad 2: (no net) -> VBAT
- L11 pad 1: Net-(L11-Pad1) -> +3V3
- L11 pad 2: VCC1V8_DDR -> Net-(C272-Pad1)
- R20 pad 2: VCC3V3_PMU -> VCC3V3_EXT
- R26 pad 2: Net-(R26-Pad2) -> VCCA1V8_PMU
- R27 pad 1: Net-(R26-Pad2) -> Net-(C275-Pad1)
- R27 pad 2: GND -> Net-(C274-Pad1)
- R56 pad 2: VCC3V3_PMU -> VCC3V3_EXT
- R57 pad 2: VCC_3V3 -> VCC3V3_EXT
- R60 pad 2: (no net) -> /HDMITX_SDA
- R61 pad 2: (no net) -> /HDMITX_SCL
- R62 pad 2: (no net) -> /HDMITX_CEC_M0
- R79 pad 1: (no net) -> Net-(J14-Pad2)
- R80 pad 1: (no net) -> Net-(J13-Pad2)
- R93 pad 2: (no net) -> Net-(J11-PadA5)
- R94 pad 2: (no net) -> Net-(J11-PadB5)
- R95 pad 2: (no net) -> Net-(J11-PadA7)
- R96 pad 2: (no net) -> Net-(J11-PadA6)
- U11 pad 15: VCC_3V3 -> VCC3V3_EXT
- U11 pad 6: VCC_3V3 -> VCC3V3_EXT
- U17 pad 1: Net-(C225-Pad1) -> VCC3V3_EXT
- U18 pad 3: (no net) -> /4G_MODULE_USB_D+
- U18 pad 4: (no net) -> /4G_MODULE_USB_D-
- U19 pad 10: (no net) -> /4G_MODULE_USB_D-
- U19 pad 22: (no net) -> Net-(J12-Pad2)
- U19 pad 23: (no net) -> Net-(J12-Pad1)
- U19 pad 52: (no net) -> VCC_3V3
- U19 pad 54: VCC_3V3 -> GND
- U19 pad 9: (no net) -> /4G_MODULE_USB_D+
- U3 pad 22: VCCIO_W -> VCCIO_WL
- U6 pad 1: +3V3 -> Net-(C278-Pad1)
- U6 pad 3: Net-(L11-Pad1) -> Net-(L14-Pad1)
- U6 pad 5: (no net) -> Net-(R103-Pad1)
- U6 pad 6: Net-(R26-Pad2) -> Net-(R104-Pad2)
- U7 pad 11: (no net) -> Net-(R28-Pad2)
